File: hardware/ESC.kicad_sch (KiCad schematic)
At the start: 93 parts, among them J1 +, J10 +, J2 -, J3 +, J4 +, J5 +, J6 +, J7 Conn_01x03, J8 +, J9 +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

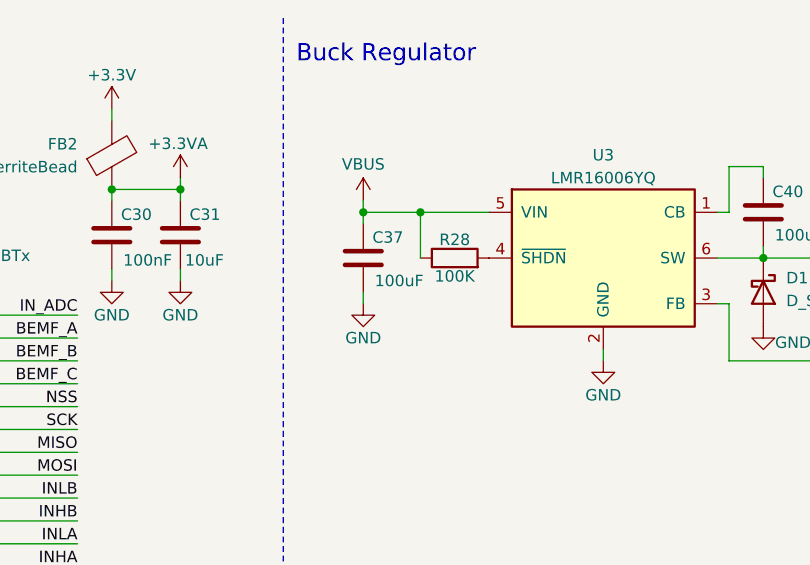
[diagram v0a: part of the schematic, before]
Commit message: fixed regulator cap value
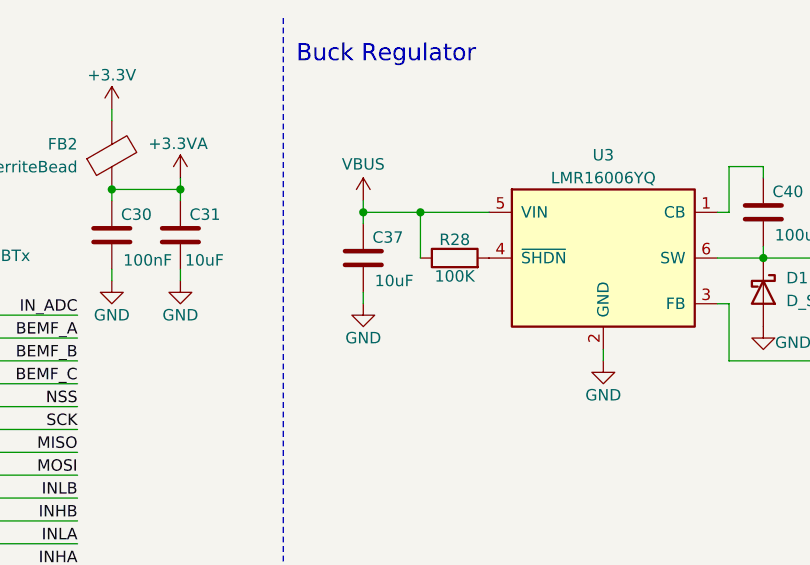
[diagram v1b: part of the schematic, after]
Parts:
- C37: value 100uF -> 10uF
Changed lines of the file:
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@@
 			)
 		)
-		(property "Value" "100uF"
+		(property "Value" "10uF"
 			(at 186.69 39.37 0)
 			(show_name no)

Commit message: made pcb layout
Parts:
- removed C35, C36: 100uF, Capacitor_SMD:C_Elec_6.3x7.7, symbol Device:C
- C37: footprint Capacitor_SMD:C_Elec_6.3x7.7 -> Capacitor_SMD:C_0603_1608Metric
- C38, C39: value 100uF -> 15uF; footprint Capacitor_SMD:C_Elec_6.3x7.7 -> Capacitor_SMD:C_0603_1608Metric
- C40, C41, C43: value 100uF -> 100nF; footprint Capacitor_SMD:C_Elec_6.3x7.7 -> Capacitor_SMD:C_0402_1005Metric
- C42: value 100uF -> 1uF; footprint Capacitor_SMD:C_Elec_6.3x7.7 -> Capacitor_SMD:C_0402_1005Metric
- C9: value 100nF -> 1uF
- L1: value 22uH -> 27uH; footprint Inductor_SMD:L_APV_ANR6020 -> Inductor_SMD:L_APV_ANR4030
- Q1, Q2, Q3, Q4, Q5, Q6: value AGM60P30AP -> AGM60P30A; footprint Package_DFN_QFN:PQFN-8-EP_6x5mm_P1.27mm_Generic -> Diode_SMD:D_QFN_3.3x3.3mm_P0.65mm
- Q7: footprint Package_DFN_QFN:PQFN-8-EP_6x5mm_P1.27mm_Generic -> Diode_SMD:D_QFN_3.3x3.3mm_P0.65mm
- R16, R18, R21, R22, R24, R26, R27: value 162K -> 226K
- R17, R19, R23, R25, R29: value 20K -> 28K
- R30: value 20K -> 8.45K
- U3: value LMR16006YQ -> LMR16006X
- U4: footprint RTA0040B -> ESC-footprints:DRV8323SRTAR
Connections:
- net +3.3V: no longer C41.1
- net at FB1.1, U4.24 (VREF): now also C41.1

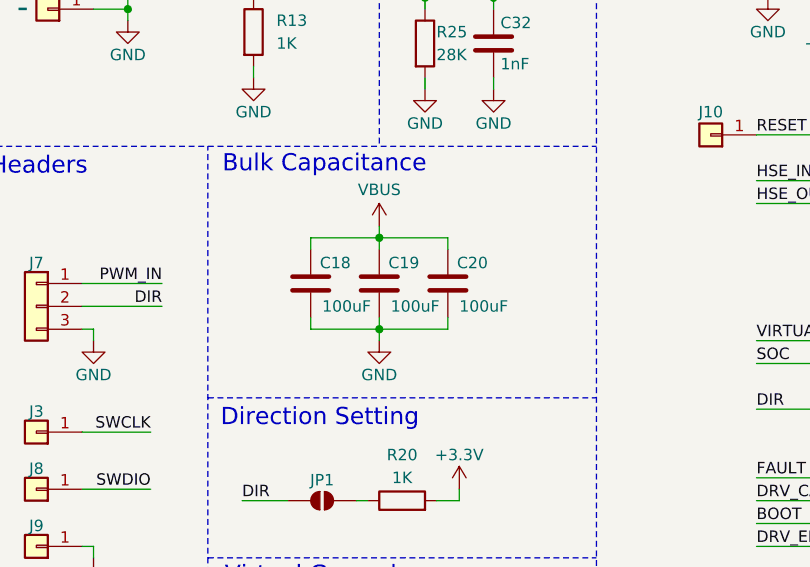
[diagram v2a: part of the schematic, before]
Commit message: added bulk capacitor
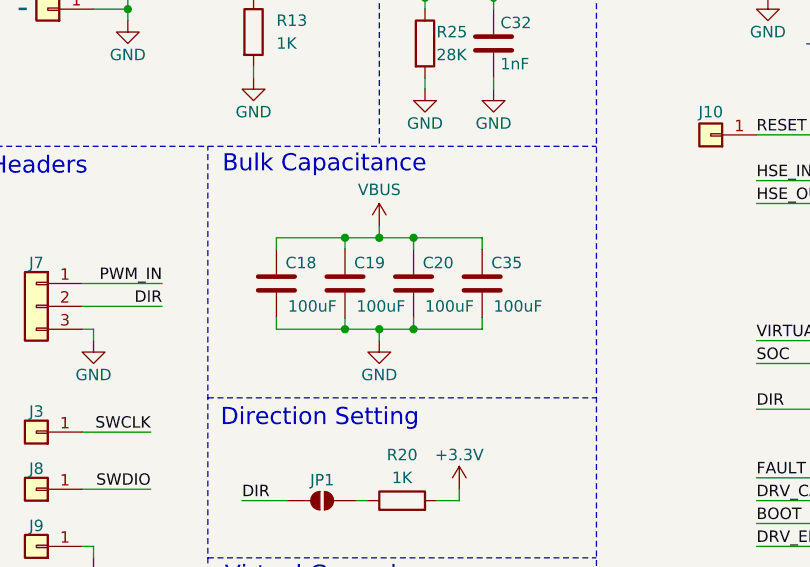
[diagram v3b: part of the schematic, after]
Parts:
- added C35: 100uF, Capacitor_SMD:C_Elec_6.3x7.7, symbol Device:C
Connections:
- net GND: now also C35.2
- net VBUS: now also C35.1
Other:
- moved on the sheet: C18, C19, C20
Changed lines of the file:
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@@
 	)
 	(junction
+		(at 59.69 59.69)
+		(diameter 0)
+		(color 0 0 0 0)
+	)
+	(junction
 		(at 129.54 118.11)
 		(diameter 0)
@@
 	)
 	(junction
+		(at 55.88 59.69)
+		(diameter 0)
+		(color 0 0 0 0)
+	)
+	(junction
 		(at 157.48 168.91)
 		(diameter 0)
@@
 	)
 	(junction
+		(at 55.88 69.85)
+		(diameter 0)
+		(color 0 0 0 0)
+	)
+	(junction
 		(at 229.87 36.83)
 		(diameter 0)
@@
 	)
 	(junction
-		(at 55.88 59.69)
+		(at 52.07 59.69)
 		(diameter 0)
 		(color 0 0 0 0)
@@
 	)
 	(junction
+		(at 59.69 69.85)
+		(diameter 0)
+		(color 0 0 0 0)
+	)
+	(junction
 		(at 261.62 36.83)
 		(diameter 0)
@@
 	)
 	(junction
-		(at 55.88 69.85)
+		(at 52.07 69.85)
 		(diameter 0)
 		(color 0 0 0 0)
@@
 	(wire
 		(pts
-			(xy 55.88 59.69) (xy 55.88 60.96)
+			(xy 52.07 59.69) (xy 52.07 60.96)
 		)
 		(stroke
@@
 	(wire
 		(pts
+			(xy 67.31 59.69) (xy 59.69 59.69)
+		)
+		(stroke
+			(width 0)
+			(type default)
+		)
+	)
+	(wire
+		(pts
 			(xy 144.78 63.5) (xy 153.67 63.5)
 		)
@@
 	(wire
 		(pts
-			(xy 55.88 68.58) (xy 55.88 69.85)
+			(xy 52.07 68.58) (xy 52.07 69.85)
 		)
 		(stroke
@@
 	(wire
 		(pts
+			(xy 55.88 59.69) (xy 52.07 59.69)
+		)
+		(stroke
+			(width 0)
+			(type default)
+		)
+	)
+	(wire
+		(pts
 			(xy 81.28 189.23) (xy 81.28 190.5)
 		)
@@
 	(wire
 		(pts
+			(xy 67.31 60.96) (xy 67.31 59.69)
+		)
+		(stroke
+			(width 0)
+			(type default)
+		)
+	)
+	(wire
+		(pts
 			(xy 165.1 27.94) (xy 165.1 29.21)
 		)
@@
 	(wire
 		(pts
-			(xy 63.5 59.69) (xy 63.5 60.96)
+			(xy 59.69 59.69) (xy 59.69 60.96)
 		)
 		(stroke
@@
 	(wire
 		(pts
-			(xy 55.88 59.69) (xy 63.5 59.69)
-		)
-		(stroke
-			(width 0)
-			(type default)
-		)
-	)
-	(wire
-		(pts
 			(xy 68.58 33.02) (xy 77.47 33.02)
 		)
@@
 	(wire
 		(pts
-			(xy 48.26 60.96) (xy 48.26 59.69)
+			(xy 44.45 60.96) (xy 44.45 59.69)
 		)
 		(stroke
@@
 	(wire
 		(pts
-			(xy 63.5 68.58) (xy 63.5 69.85)
+			(xy 59.69 68.58) (xy 59.69 69.85)
 		)
 		(stroke
@@
 	(wire
 		(pts
+			(xy 67.31 68.58) (xy 67.31 69.85)
+		)
+		(stroke
+			(width 0)
+			(type default)
+		)
+	)
+	(wire
+		(pts
 			(xy 254 36.83) (xy 254 38.1)
 		)
@@
 	(wire
 		(pts
-			(xy 48.26 68.58) (xy 48.26 69.85)
+			(xy 44.45 68.58) (xy 44.45 69.85)
 		)
 		(stroke
@@
 	(wire
 		(pts
-			(xy 48.26 69.85) (xy 55.88 69.85)
+			(xy 44.45 69.85) (xy 52.07 69.85)
 		)
 		(stroke
@@
 	(wire
 		(pts
-			(xy 55.88 69.85) (xy 63.5 69.85)
-		)
-		(stroke
-			(width 0)
-			(type default)
-		)
-	)
-	(wire
-		(pts
 			(xy 255.27 139.7) (xy 252.73 139.7)
 		)
@@
 	(wire
 		(pts
-			(xy 48.26 59.69) (xy 55.88 59.69)
+			(xy 44.45 59.69) (xy 52.07 59.69)
 		)
 		(stroke
@@
 	(wire
 		(pts
+			(xy 55.88 69.85) (xy 67.31 69.85)
+		)
+		(stroke
+			(width 0)
+			(type default)
+		)
+	)
+	(wire
+		(pts
 			(xy 157.48 97.79) (xy 157.48 99.06)
 		)
@@
 	(wire
 		(pts
+			(xy 52.07 69.85) (xy 55.88 69.85)
+		)
+		(stroke
+			(width 0)
+			(type default)
+		)
+	)
+	(wire
+		(pts
 			(xy 55.88 69.85) (xy 55.88 71.12)
 		)
@@
 	(wire
 		(pts
+			(xy 55.88 59.69) (xy 59.69 59.69)
+		)
+		(stroke
+			(width 0)
+			(type default)
+		)
+	)
+	(wire
+		(pts
 			(xy 106.68 30.48) (xy 106.68 31.75)
 		)
@@
 	(symbol
 		(lib_id "Device:C")
-		(at 63.5 64.77 0)
+		(at 59.69 64.77 0)
 		(unit 1)
 		(body_style 1)
@@
 		(dnp no)
 		(property "Reference" "C20"
-			(at 64.516 62.484 0)
+			(at 60.706 62.484 0)
 			(show_name no)
 			(do_not_autoplace no)
@@
 		)
 		(property "Value" "100uF"
-			(at 64.77 67.31 0)
+			(at 60.96 67.31 0)
 			(show_name no)
 			(do_not_autoplace no)
@@
 		)
 		(property "Footprint" "Capacitor_SMD:C_Elec_6.3x7.7"
-			(at 64.4652 68.58 0)
+			(at 60.6552 68.58 0)
 			(hide yes)
 			(show_name no)
@@
 		)
 		(property "Datasheet" ""
-			(at 63.5 64.77 0)
+			(at 59.69 64.77 0)
 			(hide yes)
 			(show_name no)
@@
 		)
 		(property "Description" "Unpolarized capacitor"
-			(at 63.5 64.77 0)
+			(at 59.69 64.77 0)
 			(hide yes)
 			(show_name no)
@@
 	(symbol
 		(lib_id "Device:C")
-		(at 55.88 64.77 0)
+		(at 52.07 64.77 0)
 		(unit 1)
 		(body_style 1)
@@
 		(dnp no)
 		(property "Reference" "C19"
-			(at 56.896 62.484 0)
+			(at 53.086 62.484 0)
 			(show_name no)
 			(do_not_autoplace no)
@@
 		)
 		(property "Value" "100uF"
-			(at 57.15 67.31 0)
+			(at 53.34 67.31 0)
 			(show_name no)
 			(do_not_autoplace no)
@@
 		)
 		(property "Footprint" "Capacitor_SMD:C_Elec_6.3x7.7"
-			(at 56.8452 68.58 0)
+			(at 53.0352 68.58 0)
 			(hide yes)
 			(show_name no)
@@
 		)
 		(property "Datasheet" ""
-			(at 55.88 64.77 0)
+			(at 52.07 64.77 0)
 			(hide yes)
 			(show_name no)
@@
 		)
 		(property "Description" "Unpolarized capacitor"
-			(at 55.88 64.77 0)
+			(at 52.07 64.77 0)
 			(hide yes)
 			(show_name no)
@@
 	)
 	(symbol
+		(lib_id "Device:C")
+		(at 67.31 64.77 0)
+		(unit 1)
+		(body_style 1)
+		(exclude_from_sim no)
+		(in_bom yes)
+		(on_board yes)
+		(in_pos_files yes)
+		(dnp no)
+		(property "Reference" "C35"
+			(at 68.326 62.484 0)
+			(show_name no)
+			(do_not_autoplace no)
+			(effects
+				(font
+					(size 1.27 1.27)
+				)
+				(justify left)
+			)
+		)
+		(property "Value" "100uF"
+			(at 68.58 67.31 0)
+			(show_name no)
+			(do_not_autoplace no)
+			(effects
+				(font
+					(size 1.27 1.27)
+				)
+				(justify left)
+			)
+		)
+		(property "Footprint" "Capacitor_SMD:C_Elec_6.3x7.7"
+			(at 68.2752 68.58 0)
+			(hide yes)
+			(show_name no)
+			(do_not_autoplace no)
+			(effects
+				(font
+					(size 1.27 1.27)
+				)
+			)
+		)
+		(property "Datasheet" ""
+			(at 67.31 64.77 0)
+			(hide yes)
+			(show_name no)
+			(do_not_autoplace no)
+			(effects
+				(font
+					(size 1.27 1.27)
+				)
+			)
+		)
+		(property "Description" "Unpolarized capacitor"
+			(at 67.31 64.77 0)
+			(hide yes)
+			(show_name no)
+			(do_not_autoplace no)
+			(effects
+				(font
+					(size 1.27 1.27)
+				)
+			)
+		)
+		(pin "1"
+		)
+		(pin "2"
+		)
+		(instances
+			(project "ESC"
+				(path "/4de1658d-a5e4-45f8-9b2f-349bf6ebe789"
+					(reference "C35")
+					(unit 1)
+				)
+			)
+		)
+	)
+	(symbol
 		(lib_id "power:GND")
 		(at 165.1 39.37 0)
@@
 	(symbol
 		(lib_id "Device:C")
-		(at 48.26 64.77 0)
+		(at 44.45 64.77 0)
 		(unit 1)
 		(body_style 1)
@@
 		(dnp no)
 		(property "Reference" "C18"
-			(at 49.276 62.484 0)
+			(at 45.466 62.484 0)
 			(show_name no)
 			(do_not_autoplace no)
@@
 		)
 		(property "Value" "100uF"
-			(at 49.53 67.31 0)
+			(at 45.72 67.31 0)
 			(show_name no)
 			(do_not_autoplace no)
@@
 		)
 		(property "Footprint" "Capacitor_SMD:C_Elec_6.3x7.7"
-			(at 49.2252 68.58 0)
+			(at 45.4152 68.58 0)
 			(hide yes)
 			(show_name no)
@@
 		)
 		(property "Datasheet" ""
-			(at 48.26 64.77 0)
+			(at 44.45 64.77 0)
 			(hide yes)
 			(show_name no)
@@
 		)
 		(property "Description" "Unpolarized capacitor"
-			(at 48.26 64.77 0)
+			(at 44.45 64.77 0)
 			(hide yes)
 			(show_name no)

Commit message: routed pcb
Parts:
- Q1, Q2, Q3, Q4, Q5, Q6: value AGM60P30A -> AGM60P30AP
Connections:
- no-connect marks 7 -> 9
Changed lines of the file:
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@@
 	)
 	(no_connect
+		(at 109.22 76.2)
+	)
+	(no_connect
 		(at 109.22 66.04)
 	)
@@
 	)
 	(no_connect
+		(at 109.22 104.14)
+	)
+	(no_connect
 		(at 109.22 96.52)
 	)
@@
 			)
 		)
-		(property "Value" "AGM60P30A"
-			(at 147.574 144.526 0)
+		(property "Value" "AGM60P30AP"
+			(at 148.59 144.272 0)
 			(show_name no)
 			(do_not_autoplace no)
@@
 			)
 		)
-		(property "Value" "AGM60P30A"
-			(at 92.964 144.78 0)
+		(property "Value" "AGM60P30AP"
+			(at 93.98 144.526 0)
 			(show_name no)
 			(do_not_autoplace no)
@@
 			)
 		)
-		(property "Value" "AGM60P30A"
-			(at 39.624 165.1 0)
+		(property "Value" "AGM60P30AP"
+			(at 40.64 164.846 0)
 			(show_name no)
 			(do_not_autoplace no)
@@
 			)
 		)
-		(property "Value" "AGM60P30A"
-			(at 39.624 144.78 0)
+		(property "Value" "AGM60P30AP"
+			(at 40.64 144.526 0)
 			(show_name no)
 			(do_not_autoplace no)
@@
 			)
 		)
-		(property "Value" "AGM60P30A"
-			(at 92.964 165.1 0)
+		(property "Value" "AGM60P30AP"
+			(at 93.98 164.846 0)
 			(show_name no)
 			(do_not_autoplace no)
@@
 			)
 		)
-		(property "Value" "AGM60P30A"
-			(at 147.574 165.1 0)
+		(property "Value" "AGM60P30AP"
+			(at 148.59 164.846 0)
 			(show_name no)
 			(do_not_autoplace no)

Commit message: touched up pcb
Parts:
- removed R32: 100K, Resistor_SMD:R_0402_1005Metric, symbol Device:R
- renumbered U4 to U1
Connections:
- net DRV_EN: now also U1.30 (ENABLE)
- net BOOT: no longer names the net of U2.45 (PB8)
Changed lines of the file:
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@@
 	(wire
 		(pts
-			(xy 97.79 91.44) (xy 109.22 91.44)
-		)
-		(stroke
-			(width 0)
-			(type default)
-		)
-	)
-	(wire
-		(pts
 			(xy 129.54 34.29) (xy 127 34.29)
 		)
@@
 	(wire
 		(pts
+			(xy 205.74 97.79) (xy 214.63 97.79)
+		)
+		(stroke
+			(width 0)
+			(type default)
+		)
+	)
+	(wire
+		(pts
 			(xy 254 45.72) (xy 254 46.99)
 		)
@@
 	(wire
 		(pts
-			(xy 205.74 97.79) (xy 207.01 97.79)
-		)
-		(stroke
-			(width 0)
-			(type default)
-		)
-	)
-	(wire
-		(pts
 			(xy 194.31 87.63) (xy 194.31 88.9)
 		)
@@
 		)
 	)
+	(label "DRV_EN"
+		(at 205.74 97.79 0)
+		(effects
+			(font
+				(size 1.27 1.27)
+			)
+			(justify left bottom)
+		)
+	)
 	(label "SWCLK"
 		(at 30.48 81.28 180)
@@
 		)
 	)
-	(label "BOOT"
-		(at 97.79 91.44 0)
-		(effects
-			(font
-				(size 1.27 1.27)
-			)
-			(justify left bottom)
-		)
-	)
 	(label "DIR"
 		(at 97.79 78.74 0)
@@
 	)
 	(symbol
-		(lib_id "Device:R")
-		(at 210.82 97.79 90)
-		(unit 1)
-		(body_style 1)
-		(exclude_from_sim no)
-		(in_bom yes)
-		(on_board yes)
-		(in_pos_files yes)
-		(dnp no)
-		(property "Reference" "R32"
-			(at 210.82 95.758 90)
-			(show_name no)
-			(do_not_autoplace no)
-			(effects
-				(font
-					(size 1.27 1.27)
-				)
-			)
-		)
-		(property "Value" "100K"
-			(at 210.82 99.822 90)
-			(show_name no)
-			(do_not_autoplace no)
-			(effects
-				(font
-					(size 1.27 1.27)
-				)
-			)
-		)
-		(property "Footprint" "Resistor_SMD:R_0402_1005Metric"
-			(at 210.82 99.568 90)
-			(hide yes)
-			(show_name no)
-			(do_not_autoplace no)
-			(effects
-				(font
-					(size 1.27 1.27)
-				)
-			)
-		)
-		(property "Datasheet" ""
-			(at 210.82 97.79 0)
-			(hide yes)
-			(show_name no)
-			(do_not_autoplace no)
-			(effects
-				(font
-					(size 1.27 1.27)
-				)
-			)
-		)
-		(property "Description" "Resistor"
-			(at 210.82 97.79 0)
-			(hide yes)
-			(show_name no)
-			(do_not_autoplace no)
-			(effects
-				(font
-					(size 1.27 1.27)
-				)
-			)
-		)
-		(pin "1"
-		)
-		(pin "2"
-		)
-		(instances
-			(project "ESC"
-				(path "/4de1658d-a5e4-45f8-9b2f-349bf6ebe789"
-					(reference "R32")
-					(unit 1)
-				)
-			)
-		)
-	)
-	(symbol
 		(lib_id "power:GND")
 		(at 185.42 41.91 0)
@@
 	)
 	(symbol
-		(lib_id "power:+3.3V")
-		(at 205.74 97.79 0)
-		(unit 1)
-		(body_style 1)
-		(exclude_from_sim no)
-		(in_bom yes)
-		(on_board yes)
-		(in_pos_files yes)
-		(dnp no)
-		(property "Reference" "#PWR066"
-			(at 205.74 101.6 0)
-			(hide yes)
-			(show_name no)
-			(do_not_autoplace no)
-			(effects
-				(font
-					(size 1.27 1.27)
-				)
-			)
-		)
-		(property "Value" "+3.3V"
-			(at 205.74 93.98 0)
-			(show_name no)
-			(do_not_autoplace no)
-			(effects
-				(font
-					(size 1.27 1.27)
-				)
-			)
-		)
-		(property "Footprint" ""
-			(at 205.74 97.79 0)
-			(hide yes)
-			(show_name no)
-			(do_not_autoplace no)
-			(effects
-				(font
-					(size 1.27 1.27)
-				)
-			)
-		)
-		(property "Datasheet" ""
-			(at 205.74 97.79 0)
-			(hide yes)
-			(show_name no)
-			(do_not_autoplace no)
-			(effects
-				(font
-					(size 1.27 1.27)
-				)
-			)
-		)
-		(property "Description" "Power symbol creates a global label with name \"+3.3V\""
-			(at 205.74 97.79 0)
-			(hide yes)
-			(show_name no)
-			(do_not_autoplace no)
-			(effects
-				(font
-					(size 1.27 1.27)
-				)
-			)
-		)
-		(pin "1"
-		)
-		(instances
-			(project "ESC"
-				(path "/4de1658d-a5e4-45f8-9b2f-349bf6ebe789"
-					(reference "#PWR066")
-					(unit 1)
-				)
-			)
-		)
-	)
-	(symbol
 		(lib_id "power:GND")
 		(at 125.73 118.11 0)
@@
 		(dnp no)
 		(fields_autoplaced yes)
-		(property "Reference" "U4"
+		(property "Reference" "U1"
 			(at 233.045 78.74 0)
 			(show_name no)
@@
 			(project "ESC"
 				(path "/4de1658d-a5e4-45f8-9b2f-349bf6ebe789"
-					(reference "U4")
+					(reference "U1")
 					(unit 1)
 				)
